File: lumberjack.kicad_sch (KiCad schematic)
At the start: 155 parts, among them J1 USB, J2 AVR_ISP_6, J3 JST, J4 JST, SW1 RESET, SW2 BOOT, U1 ATMEGA328-PU, Y1 16MHz

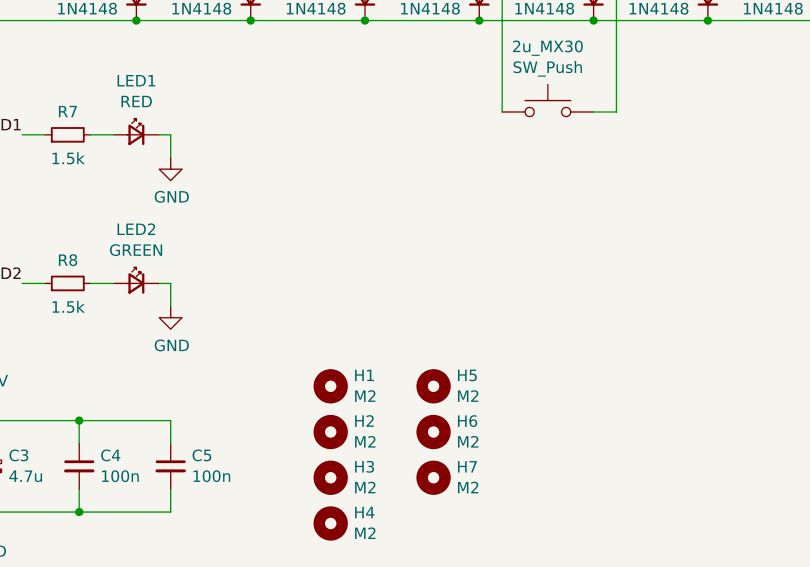
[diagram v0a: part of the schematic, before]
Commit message: Add extra standoff mounting holes
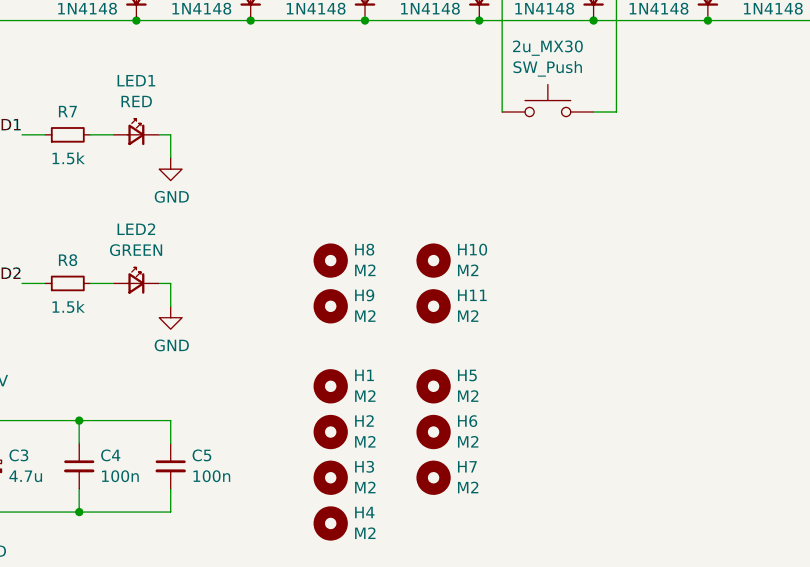
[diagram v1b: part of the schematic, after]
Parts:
- added H10, H11, H8, H9: M2, lumberjack:MountingHole_M2, symbol Mechanical:MountingHole
- J1: footprint lumberjack:USB_Hybrid -> lumberjack:USB_Hybrid_THT
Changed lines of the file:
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@@
     (property "Reference" "J1" (id 0) (at 31.9278 23.6982 0))
     (property "Value" "USB" (id 1) (at 31.9278 26.0096 0))
-    (property "Footprint" "lumberjack:USB_Hybrid" (id 2) (at 33.02 45.72 0)
+    (property "Footprint" "lumberjack:USB_Hybrid_THT" (id 2) (at 33.02 45.72 0)
       (effects (font (size 1.27 1.27)) hide)
     )
@@
     (pin "1")
   )
+  (symbol (lib_id "Mechanical:MountingHole") (at 156.21 167.64 0) (unit 1)
+    (in_bom yes) (on_board yes)
+    (property "Reference" "H9" (id 0) (at 158.75 166.4716 0)
+      (effects (font (size 1.27 1.27)) (justify left))
+    )
+    (property "Value" "M2" (id 1) (at 158.75 168.783 0)
+      (effects (font (size 1.27 1.27)) (justify left))
+    )
+    (property "Footprint" "lumberjack:MountingHole_M2" (id 2) (at 156.21 167.64 0)
+      (effects (font (size 1.27 1.27)) hide)
+    )
+    (property "Datasheet" "~" (id 3) (at 156.21 167.64 0)
+      (effects (font (size 1.27 1.27)) hide)
+    )
+  )
+  (symbol (lib_id "Mechanical:MountingHole") (at 156.21 162.56 0) (unit 1)
+    (in_bom yes) (on_board yes)
+    (property "Reference" "H8" (id 0) (at 158.75 161.3916 0)
+      (effects (font (size 1.27 1.27)) (justify left))
+    )
+    (property "Value" "M2" (id 1) (at 158.75 163.703 0)
+      (effects (font (size 1.27 1.27)) (justify left))
+    )
+    (property "Footprint" "lumberjack:MountingHole_M2" (id 2) (at 156.21 162.56 0)
+      (effects (font (size 1.27 1.27)) hide)
+    )
+    (property "Datasheet" "~" (id 3) (at 156.21 162.56 0)
+      (effects (font (size 1.27 1.27)) hide)
+    )
+  )
+  (symbol (lib_id "Mechanical:MountingHole") (at 167.64 167.64 0) (unit 1)
+    (in_bom yes) (on_board yes)
+    (property "Reference" "H11" (id 0) (at 170.18 166.4716 0)
+      (effects (font (size 1.27 1.27)) (justify left))
+    )
+    (property "Value" "M2" (id 1) (at 170.18 168.783 0)
+      (effects (font (size 1.27 1.27)) (justify left))
+    )
+    (property "Footprint" "lumberjack:MountingHole_M2" (id 2) (at 167.64 167.64 0)
+      (effects (font (size 1.27 1.27)) hide)
+    )
+    (property "Datasheet" "~" (id 3) (at 167.64 167.64 0)
+      (effects (font (size 1.27 1.27)) hide)
+    )
+  )
+  (symbol (lib_id "Mechanical:MountingHole") (at 167.64 162.56 0) (unit 1)
+    (in_bom yes) (on_board yes)
+    (property "Reference" "H10" (id 0) (at 170.18 161.3916 0)
+      (effects (font (size 1.27 1.27)) (justify left))
+    )
+    (property "Value" "M2" (id 1) (at 170.18 163.703 0)
+      (effects (font (size 1.27 1.27)) (justify left))
+    )
+    (property "Footprint" "lumberjack:MountingHole_M2" (id 2) (at 167.64 162.56 0)
+      (effects (font (size 1.27 1.27)) hide)
+    )
+    (property "Datasheet" "~" (id 3) (at 167.64 162.56 0)
+      (effects (font (size 1.27 1.27)) hide)
+    )
+  )
   (sheet_instances
     (path "/" (page "1"))
@@
       (reference "H7") (unit 1) (value "M2") (footprint "lumberjack:MountingSlot_M2")
     )
+    (path "/25e26648-7633-4c68-93e4-868433452d01"
+      (reference "H8") (unit 1) (value "M2") (footprint "lumberjack:MountingHole_M2")
+    )
+    (path "/07ccd3f7-ee44-46b1-947b-cb6859caff1a"
+      (reference "H9") (unit 1) (value "M2") (footprint "lumberjack:MountingHole_M2")
+    )
+    (path "/adc89143-18a4-4268-89ab-568e66a6e610"
+      (reference "H10") (unit 1) (value "M2") (footprint "lumberjack:MountingHole_M2")
+    )
+    (path "/7d35b34a-6c33-4331-bd17-b3f940094af3"
+      (reference "H11") (unit 1) (value "M2") (footprint "lumberjack:MountingHole_M2")
+    )
     (path "/00000000-0000-0000-0000-0000601e2e5d"
-      (reference "J1") (unit 1) (value "USB") (footprint "lumberjack:USB_Hybrid")
+      (reference "J1") (unit 1) (value "USB") (footprint "lumberjack:USB_Hybrid_THT")
     )
     (path "/00000000-0000-0000-0000-00005c3f2fd0"
